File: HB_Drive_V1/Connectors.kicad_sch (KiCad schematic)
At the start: 56 parts, among them J501 54-00164, J502 5227699-1, J503 USB-B-S-X-X-VT, J505 Conn_01x03, J506 30306-6002HB, U501 REF102CU, U502 R-78E5.0-0.5, U503 TL082, U504 TL082, U505 TMH 0515D, U506 AMS1117-3.3

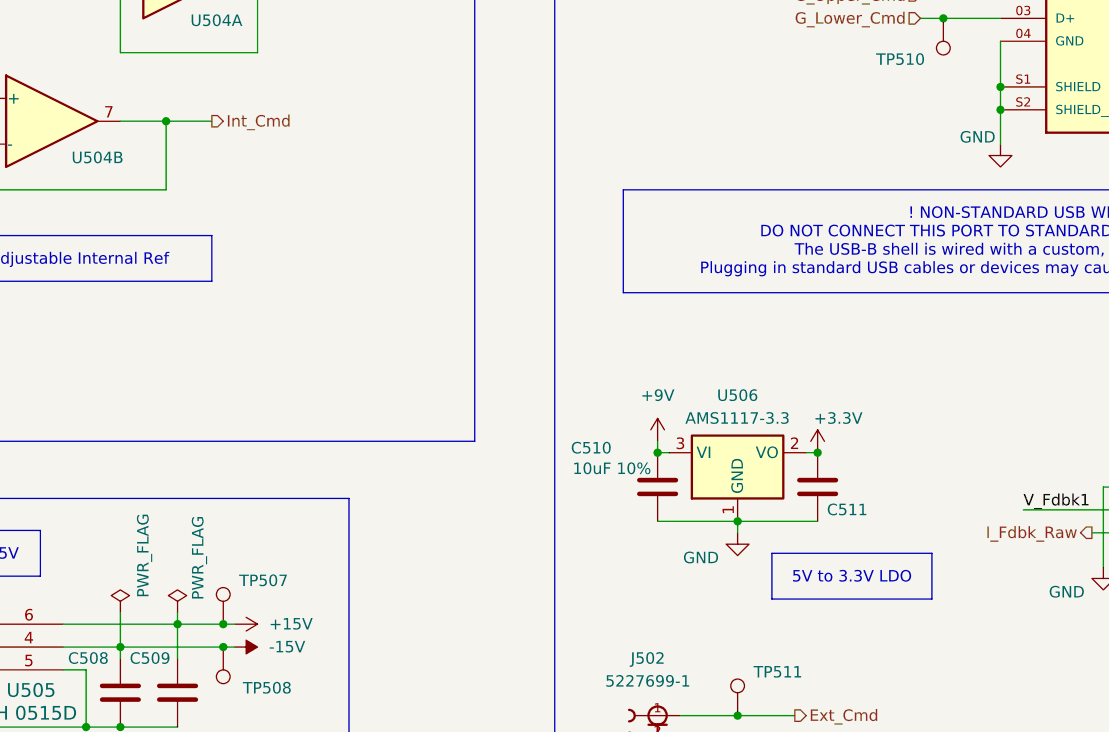
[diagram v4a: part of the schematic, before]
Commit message: Updates to 1st review corrected V2 of board
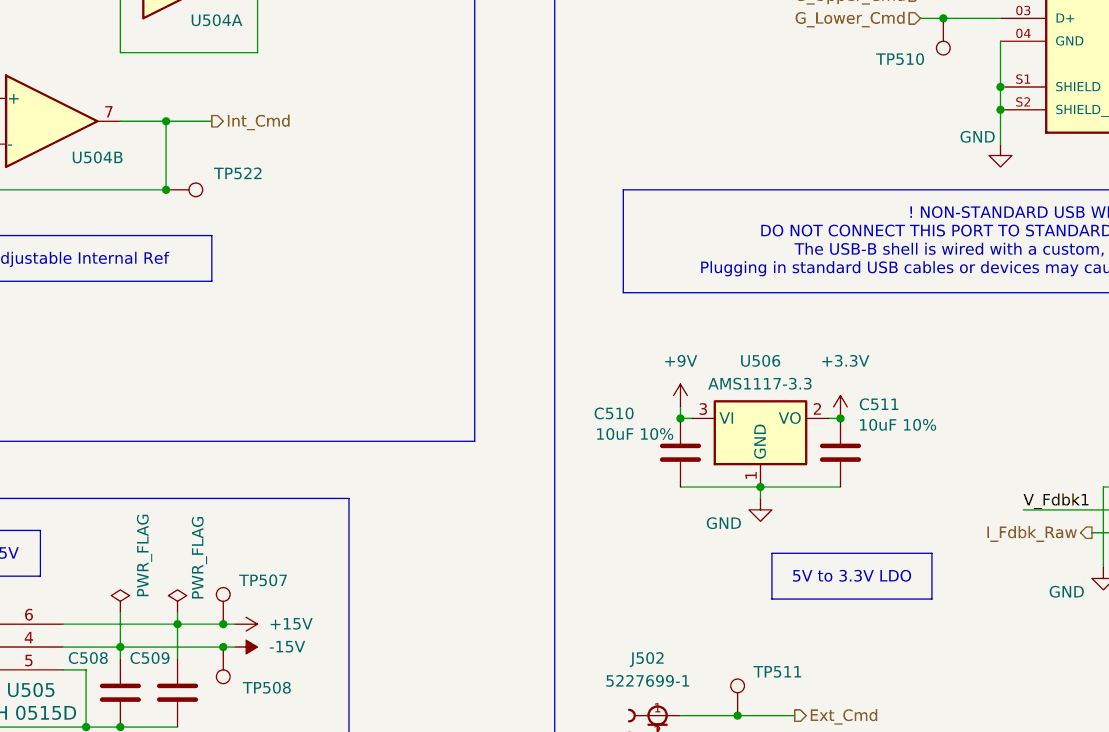
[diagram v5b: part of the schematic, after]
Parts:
- added TP522: TestPoint, TestPoint:TestPoint_Loop_D2.60mm_Drill1.6mm_Beaded, symbol Connector:TestPoint
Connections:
- net Int_Cmd: now also TP522.1
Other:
- moved on the sheet: C510, C511, U506
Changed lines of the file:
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@@
 	)
 	(junction
-		(at 264.16 113.03)
+		(at 266.7 109.22)
 		(diameter 0)
 		(color 0 0 0 0)
@@
 	)
 	(junction
-		(at 255.27 105.41)
+		(at 257.81 101.6)
 		(diameter 0)
 		(color 0 0 0 0)
@@
 	)
 	(junction
+		(at 200.66 76.2)
+		(diameter 0)
+		(color 0 0 0 0)
+	)
+	(junction
 		(at 311.15 186.69)
 		(diameter 0)
@@
 	)
 	(junction
-		(at 273.05 105.41)
+		(at 275.59 101.6)
 		(diameter 0)
 		(color 0 0 0 0)
@@
 	(wire
 		(pts
-			(xy 255.27 105.41) (xy 256.54 105.41)
+			(xy 257.81 101.6) (xy 259.08 101.6)
 		)
 		(stroke
@@
 	(wire
 		(pts
-			(xy 255.27 113.03) (xy 264.16 113.03)
+			(xy 257.81 109.22) (xy 266.7 109.22)
 		)
 		(stroke
@@
 	(wire
 		(pts
-			(xy 264.16 113.03) (xy 273.05 113.03)
+			(xy 266.7 109.22) (xy 275.59 109.22)
 		)
 		(stroke
@@
 	(wire
 		(pts
-			(xy 255.27 104.14) (xy 255.27 105.41)
+			(xy 257.81 100.33) (xy 257.81 101.6)
 		)
 		(stroke
@@
 	(wire
 		(pts
-			(xy 264.16 114.3) (xy 264.16 113.03)
+			(xy 266.7 110.49) (xy 266.7 109.22)
 		)
 		(stroke
@@
 	(wire
 		(pts
-			(xy 273.05 105.41) (xy 271.78 105.41)
+			(xy 275.59 101.6) (xy 274.32 101.6)
 		)
 		(stroke
@@
 	(symbol
 		(lib_id "Connector:TestPoint")
+		(at 200.66 76.2 270)
+		(unit 1)
+		(body_style 1)
+		(exclude_from_sim no)
+		(in_bom yes)
+		(on_board yes)
+		(in_pos_files yes)
+		(dnp no)
+		(property "Reference" "TP522"
+			(at 205.994 74.422 90)
+			(show_name no)
+			(do_not_autoplace no)
+			(effects
+				(font
+					(size 1.27 1.27)
+				)
+				(justify left)
+			)
+		)
+		(property "Value" "TestPoint"
+			(at 202.6921 78.74 0)
+			(hide yes)
+			(show_name no)
+			(do_not_autoplace no)
+			(effects
+				(font
+					(size 1.27 1.27)
+				)
+				(justify left)
+			)
+		)
+		(property "Footprint" "TestPoint:TestPoint_Loop_D2.60mm_Drill1.6mm_Beaded"
+			(at 200.66 81.28 0)
+			(hide yes)
+			(show_name no)
+			(do_not_autoplace no)
+			(effects
+				(font
+					(size 1.27 1.27)
+				)
+			)
+		)
+		(property "Datasheet" ""
+			(at 200.66 81.28 0)
+			(hide yes)
+			(show_name no)
+			(do_not_autoplace no)
+			(effects
+				(font
+					(size 1.27 1.27)
+				)
+			)
+		)
+		(property "Description" "test point"
+			(at 200.66 76.2 0)
+			(hide yes)
+			(show_name no)
+			(do_not_autoplace no)
+			(effects
+				(font
+					(size 1.27 1.27)
+				)
+			)
+		)
+		(property "Sim.Device" ""
+			(at 200.66 76.2 0)
+			(hide yes)
+			(show_name no)
+			(do_not_autoplace no)
+			(effects
+				(font
+					(size 1.27 1.27)
+				)
+			)
+		)
+		(pin "1"
+		)
+		(instances
+			(project "HB_Drive_V1"
+				(path "/a9b54c89-4c8e-4c90-8a0d-ec2009e369b7/affa1a72-7fee-4831-b027-79a553ce267b"
+					(reference "TP522")
+					(unit 1)
+				)
+			)
+		)
+	)
+	(symbol
+		(lib_id "Connector:TestPoint")
 		(at 143.51 49.53 0)
 		(unit 1)
@@
 	(symbol
 		(lib_id "Device:C")
-		(at 273.05 109.22 0)
+		(at 275.59 105.41 0)
 		(mirror y)
 		(unit 1)
@@
 		(dnp no)
 		(property "Reference" "C511"
-			(at 276.352 111.76 0)
+			(at 279.908 100.076 0)
 			(show_name no)
 			(do_not_autoplace no)
@@
 		)
 		(property "Value" "10uF 10%"
-			(at 277.622 107.442 0)
-			(hide yes)
+			(at 281.94 102.362 0)
 			(show_name no)
 			(do_not_autoplace no)
@@
 		)
 		(property "Footprint" "Capacitor_SMD:C_0603_1608Metric"
-			(at 272.0848 113.03 0)
+			(at 274.6248 109.22 0)
 			(hide yes)
 			(show_name no)
@@
 		)
 		(property "Datasheet" ""
-			(at 273.05 109.22 0)
+			(at 275.59 105.41 0)
 			(hide yes)
 			(show_name no)
@@
 		)
 		(property "Description" "Unpolarized capacitor"
-			(at 273.05 109.22 0)
+			(at 275.59 105.41 0)
 			(hide yes)
 			(show_name no)
@@
 		)
 		(property "Sim.Device" ""
-			(at 273.05 109.22 0)
+			(at 275.59 105.41 0)
 			(hide yes)
 			(show_name no)
@@
 	(symbol
 		(lib_id "power:+3.3V")
-		(at 273.05 105.41 0)
+		(at 275.59 101.6 0)
 		(unit 1)
 		(body_style 1)
@@
 		(dnp no)
 		(property "Reference" "#PWR0529"
-			(at 273.05 109.22 0)
+			(at 275.59 105.41 0)
 			(hide yes)
 			(show_name no)
@@
 		)
 		(property "Value" "+3.3V"
-			(at 275.336 101.6 0)
+			(at 276.098 95.25 0)
 			(show_name no)
 			(do_not_autoplace no)
@@
 		)
 		(property "Footprint" ""
-			(at 273.05 105.41 0)
+			(at 275.59 101.6 0)
 			(hide yes)
 			(show_name no)
@@
 		)
 		(property "Datasheet" ""
-			(at 273.05 105.41 0)
+			(at 275.59 101.6 0)
 			(hide yes)
 			(show_name no)
@@
 		)
 		(property "Description" "Power symbol creates a global label with name \"+3.3V\""
-			(at 273.05 105.41 0)
+			(at 275.59 101.6 0)
 			(hide yes)
 			(show_name no)
@@
 	(symbol
 		(lib_id "power:GND")
-		(at 264.16 114.3 0)
+		(at 266.7 110.49 0)
 		(unit 1)
 		(body_style 1)
@@
 		(dnp no)
 		(property "Reference" "#PWR0528"
-			(at 264.16 120.65 0)
+			(at 266.7 116.84 0)
 			(hide yes)
 			(show_name no)
@@
 		)
 		(property "Value" "GND"
-			(at 260.096 117.094 0)
+			(at 262.636 113.284 0)
 			(show_name no)
 			(do_not_autoplace no)
@@
 		)
 		(property "Footprint" ""
-			(at 264.16 114.3 0)
+			(at 266.7 110.49 0)
 			(hide yes)
 			(show_name no)
@@
 		)
 		(property "Datasheet" ""
-			(at 264.16 114.3 0)
+			(at 266.7 110.49 0)
 			(hide yes)
 			(show_name no)
@@
 		)
 		(property "Description" "Power symbol creates a global label with name \"GND\" , ground"
-			(at 264.16 114.3 0)
+			(at 266.7 110.49 0)
 			(hide yes)
 			(show_name no)
@@
 	(symbol
 		(lib_id "Regulator_Linear:AMS1117-3.3")
-		(at 264.16 105.41 0)
+		(at 266.7 101.6 0)
 		(unit 1)
 		(body_style 1)
@@
 		(fields_autoplaced yes)
 		(property "Reference" "U506"
-			(at 264.16 99.06 0)
+			(at 266.7 95.25 0)
 			(show_name no)
 			(do_not_autoplace no)
@@
 		)
 		(property "Value" "AMS1117-3.3"
-			(at 264.16 101.6 0)
+			(at 266.7 97.79 0)
 			(show_name no)
 			(do_not_autoplace no)
@@
 		)
 		(property "Footprint" "Package_TO_SOT_SMD:SOT-223-3_TabPin2"
-			(at 264.16 100.33 0)
+			(at 266.7 96.52 0)
 			(hide yes)
 			(show_name no)
@@
 		)
 		(property "Datasheet" "http://www.advanced-monolithic.com/pdf/ds1117.pdf"
-			(at 266.7 111.76 0)
+			(at 269.24 107.95 0)
 			(hide yes)
 			(show_name no)
@@
 		)
 		(property "Description" "1A Low Dropout regulator, positive, 3.3V fixed output, SOT-223"
-			(at 264.16 105.41 0)
+			(at 266.7 101.6 0)
 			(hide yes)
 			(show_name no)
@@
 		)
 		(property "Sim.Device" ""
-			(at 264.16 105.41 0)
+			(at 266.7 101.6 0)
 			(hide yes)
 			(show_name no)
@@
 	(symbol
 		(lib_id "power:+9V")
-		(at 255.27 104.14 0)
+		(at 257.81 100.33 0)
 		(unit 1)
 		(body_style 1)
@@
 		(fields_autoplaced yes)
 		(property "Reference" "#PWR0527"
-			(at 255.27 107.95 0)
+			(at 257.81 104.14 0)
 			(hide yes)
 			(show_name no)
@@
 		)
 		(property "Value" "+9V"
-			(at 255.27 99.06 0)
+			(at 257.81 95.25 0)
 			(show_name no)
 			(do_not_autoplace no)
@@
 		)
 		(property "Footprint" ""
-			(at 255.27 104.14 0)
+			(at 257.81 100.33 0)
 			(hide yes)
 			(show_name no)
@@
 		)
 		(property "Datasheet" ""
-			(at 255.27 104.14 0)
+			(at 257.81 100.33 0)
 			(hide yes)
 			(show_name no)
@@
 		)
 		(property "Description" "Power symbol creates a global label with name \"+9V\""
-			(at 255.27 104.14 0)
+			(at 257.81 100.33 0)
 			(hide yes)
 			(show_name no)
@@
 	(symbol
 		(lib_id "Device:C")
-		(at 255.27 109.22 0)
+		(at 257.81 105.41 0)
 		(unit 1)
 		(body_style 1)
@@
 		(dnp no)
 		(property "Reference" "C510"
-			(at 247.904 104.902 0)
+			(at 250.444 101.092 0)
 			(show_name no)
 			(do_not_autoplace no)
@@
 		)
 		(property "Value" "10uF 10%"
-			(at 250.19 107.188 0)
+			(at 252.73 103.378 0)
 			(show_name no)
 			(do_not_autoplace no)
@@
 		)
 		(property "Footprint" "Capacitor_SMD:C_0603_1608Metric"
-			(at 256.2352 113.03 0)
+			(at 258.7752 109.22 0)
 			(hide yes)
 			(show_name no)
@@
 		)
 		(property "Datasheet" ""
-			(at 255.27 109.22 0)
+			(at 257.81 105.41 0)
 			(hide yes)
 			(show_name no)
@@
 		)
 		(property "Description" "Unpolarized capacitor"
-			(at 255.27 109.22 0)
+			(at 257.81 105.41 0)
 			(hide yes)
 			(show_name no)
@@
 		)
 		(property "Sim.Device" ""
-			(at 255.27 109.22 0)
+			(at 257.81 105.41 0)
 			(hide yes)
 			(show_name no)

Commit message: restores v2 to condtion as ordered!
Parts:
- U501: value REF102CU -> REF102AU
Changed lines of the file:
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@@
 			)
 		)
-		(property "Value" "REF102CU"
+		(property "Value" "REF102AU"
 			(at 101.2033 49.53 0)
 			(show_name no)

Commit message: Moves Ports and adds level shifter
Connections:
- net +3.3V: no longer J506.2
- net +5V: now also C510.1, U506.3 (VI)
- net +9V: no longer C510.1, U506.3 (VI)
- net GND: now also J506.2
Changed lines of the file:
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@@
 	)
 	(junction
+		(at 334.01 114.3)
+		(diameter 0)
+		(color 0 0 0 0)
+	)
+	(junction
 		(at 257.81 101.6)
 		(diameter 0)
@@
 	(wire
 		(pts
-			(xy 334.01 104.14) (xy 334.01 109.22)
+			(xy 127 67.31) (xy 143.51 67.31)
 		)
 		(stroke
@@
 	(wire
 		(pts
-			(xy 127 67.31) (xy 143.51 67.31)
+			(xy 334.01 114.3) (xy 334.01 118.11)
 		)
 		(stroke
@@
 	(wire
 		(pts
-			(xy 334.01 114.3) (xy 334.01 118.11)
+			(xy 177.8 71.12) (xy 177.8 76.2)
 		)
 		(stroke
@@
 	(wire
 		(pts
-			(xy 177.8 71.12) (xy 177.8 76.2)
+			(xy 264.16 137.16) (xy 269.24 137.16)
 		)
 		(stroke
@@
 	(wire
 		(pts
-			(xy 264.16 137.16) (xy 269.24 137.16)
+			(xy 334.01 109.22) (xy 334.01 114.3)
 		)
 		(stroke
@@
 	)
 	(symbol
-		(lib_id "power:+3.3V")
-		(at 334.01 104.14 0)
-		(unit 1)
-		(body_style 1)
-		(exclude_from_sim no)
-		(in_bom yes)
-		(on_board yes)
-		(in_pos_files yes)
-		(dnp no)
-		(property "Reference" "#PWR0537"
-			(at 334.01 107.95 0)
-			(hide yes)
-			(show_name no)
-			(do_not_autoplace no)
-			(effects
-				(font
-					(size 1.27 1.27)
-				)
-			)
-		)
-		(property "Value" "+3.3V"
-			(at 336.296 100.33 0)
-			(show_name no)
-			(do_not_autoplace no)
-			(effects
-				(font
-					(size 1.27 1.27)
-				)
-			)
-		)
-		(property "Footprint" ""
-			(at 334.01 104.14 0)
-			(hide yes)
-			(show_name no)
-			(do_not_autoplace no)
-			(effects
-				(font
-					(size 1.27 1.27)
-				)
-			)
-		)
-		(property "Datasheet" ""
-			(at 334.01 104.14 0)
-			(hide yes)
-			(show_name no)
-			(do_not_autoplace no)
-			(effects
-				(font
-					(size 1.27 1.27)
-				)
-			)
-		)
-		(property "Description" "Power symbol creates a global label with name \"+3.3V\""
-			(at 334.01 104.14 0)
-			(hide yes)
-			(show_name no)
-			(do_not_autoplace no)
-			(effects
-				(font
-					(size 1.27 1.27)
-				)
-			)
-		)
-		(pin "1"
-		)
-		(instances
-			(project "HB_Drive_V1"
-				(path "/a9b54c89-4c8e-4c90-8a0d-ec2009e369b7/affa1a72-7fee-4831-b027-79a553ce267b"
-					(reference "#PWR0537")
-					(unit 1)
-				)
-			)
-		)
-	)
-	(symbol
 		(lib_id "power:GND")
 		(at 293.37 71.12 0)
@@
 		(in_pos_files yes)
 		(dnp no)
-		(fields_autoplaced yes)
 		(property "Reference" "#PWR0527"
 			(at 257.81 104.14 0)
@@
 			)
 		)
-		(property "Value" "+9V"
-			(at 257.81 95.25 0)
+		(property "Value" "+5V"
+			(at 255.778 96.266 0)
 			(show_name no)
 			(do_not_autoplace no)
@@
 					(size 1.27 1.27)
 				)
+				(justify left)
 			)
 		)

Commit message: Brings everything up to latest copy on my computer
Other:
- company: (none) -> UW Madison, WEMPEC
- title: (none) -> HB Drive V3
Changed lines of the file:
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@@
 	(generator_version "10.0")
 	(paper "A3")
+	(title_block
+		(title "HB Drive V3")
+		(date "2026-09-08")
+		(company "UW Madison, WEMPEC")
+	)
 	(rectangle
 		(start 243.84 165.1)
